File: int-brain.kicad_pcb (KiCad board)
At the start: 2 copper layers, 117.4 x 66.6 mm, 62 parts, among them J1 PWR, J10 Conn_01x19_Pin, J11 Conn_01x19_Pin, J2 UART0, J3 I2C0, J4 PWR, J5 1MA, J6 1MB, J7 2MA, J8 2MB, J9 MPU9250, U1 L298N, U2 ESP32-DevKitC, U3 L298N, U4 LM2576HVT-5

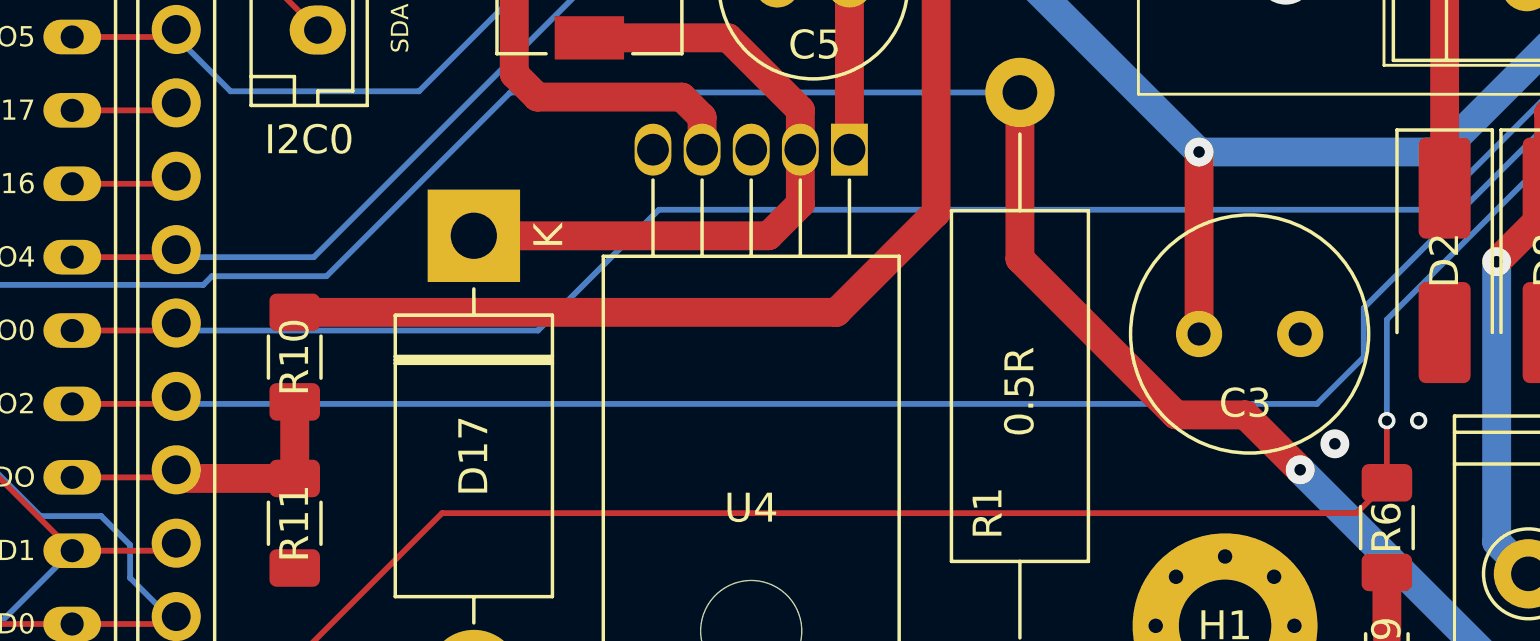
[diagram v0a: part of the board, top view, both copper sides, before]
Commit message: re-do pinouts based on code
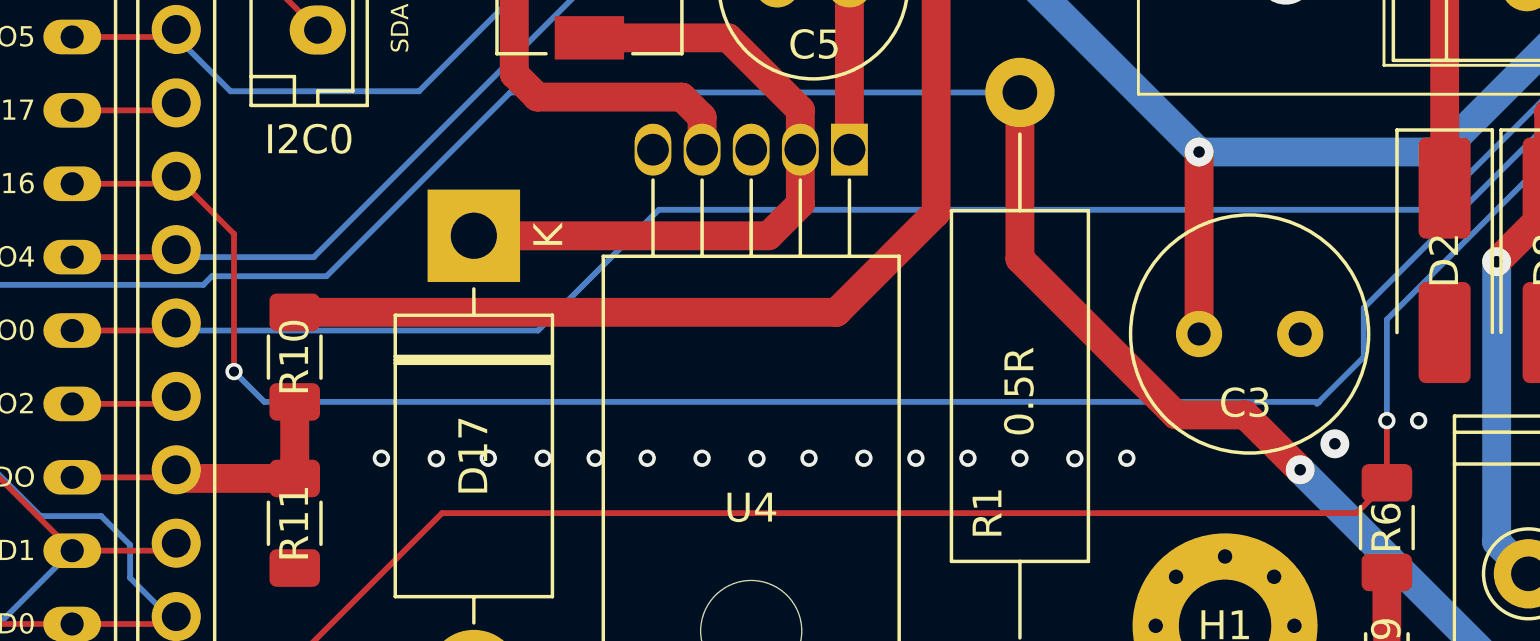
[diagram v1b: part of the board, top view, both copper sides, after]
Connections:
- J11 pad 12: /GPIO16 -> 1MA2_IN
- J11 pad 15: 1MA2_IN -> /GPIO2
- U2 pad 24: 1MA2_IN -> /GPIO2
- U2 pad 27: /GPIO16 -> 1MA2_IN
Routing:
- net 1MA2_IN: track 72.2 -> 78.3 mm, vias 0 -> 1
- net /GPIO2: track 0.00 -> 3.60 mm
- net /GPIO16: track 3.60 -> 0.00 mm
- net GND: vias 54 -> 69

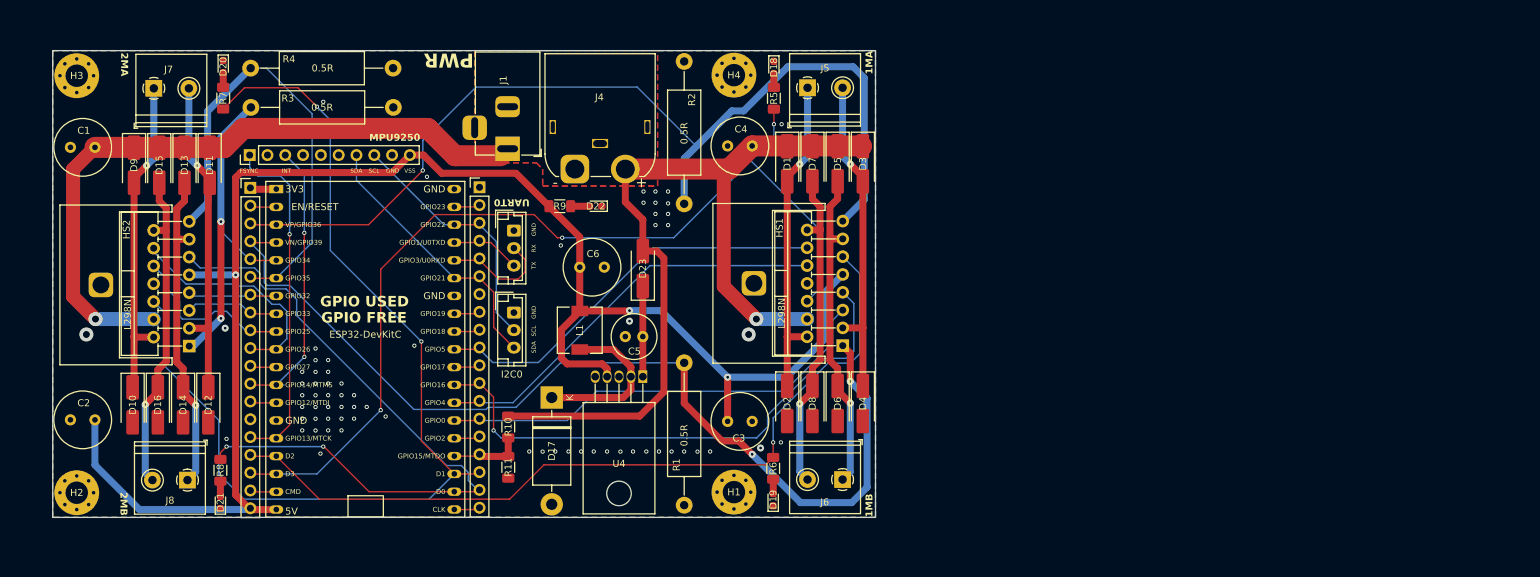
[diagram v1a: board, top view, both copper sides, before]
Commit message: finish schematic rearrangement
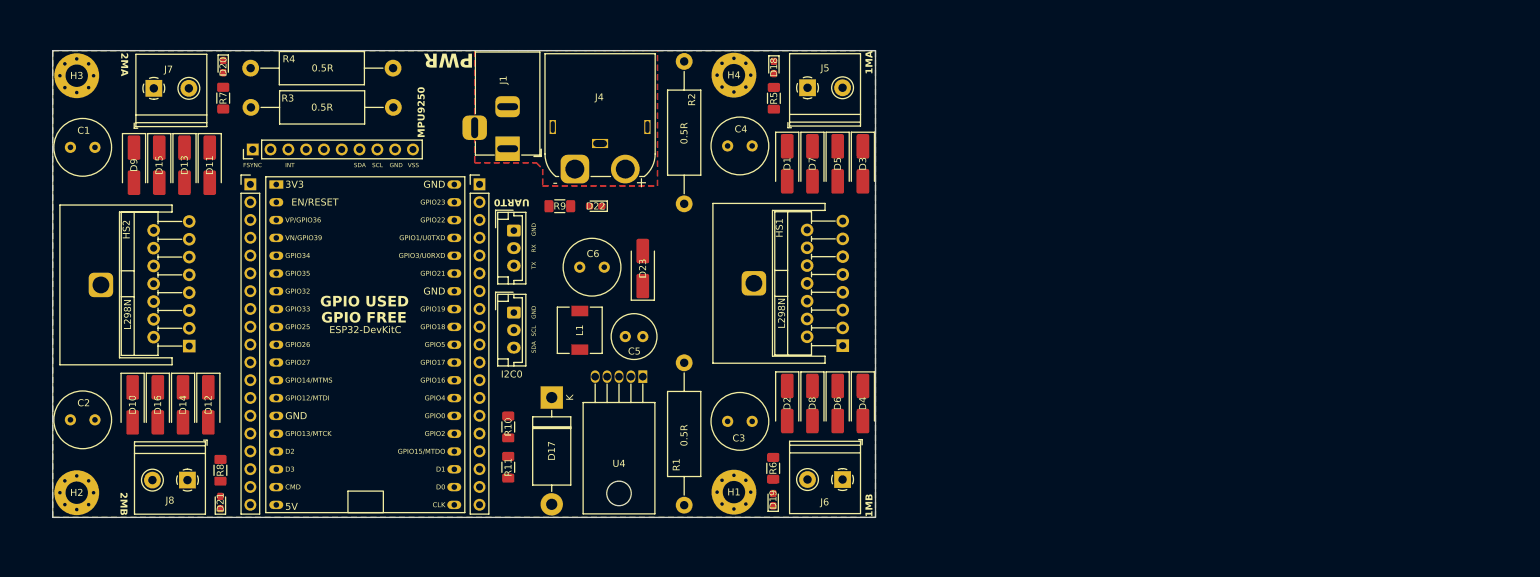
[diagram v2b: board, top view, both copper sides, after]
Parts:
- J10: value Conn_01x19_Pin -> Left
- J11: value Conn_01x19_Pin -> Right
- moved J9 0.91 mm to (88.9, 62.5)
- moved U2 0.66 mm to (92.3, 67.5)
- moved J10 0.50 mm to (88.6, 67.5)
- moved J11 0.42 mm to (121.3, 67.5)
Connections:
- net /CHIP_PU renamed /EN
- net /CMD renamed /GPIO11
- J10 pad 10: 2MB2_IN -> 2MA2_IN
- J10 pad 11: /GPIO27 -> 2MA_EN
- J10 pad 12: INT -> 2MA1_IN
- J10 pad 13: /GPIO12 -> FSYNC
- J10 pad 14: unconnected-(J10-Pin_14-Pad14) -> GND
- J10 pad 15: FSYNC -> INT
- J10 pad 16: 1MB_EN -> /GPIO9
- J10 pad 17: 1MA_EN -> /GPIO10
- J10 pad 3: 1MB_SENSE -> /GPIO36
- J10 pad 4: 1MA_SENSE -> VBATT
- J10 pad 7: 2MA2_IN -> 2MB2_IN
- J10 pad 8: 2MA1_IN -> 2MB_EN
- J11 pad 10: 1MB2_IN -> 1MA2_IN
- J11 pad 11: /GPIO17 -> 1MA_EN
- J11 pad 12: 1MA2_IN -> 1MA1_IN
- J11 pad 13: 1MB1_IN -> 1MB_SENSE
- J11 pad 14: 1MA1_IN -> /GPIO0
- J11 pad 16: VBATT -> 1MA_SENSE
- J11 pad 17: 2MA_EN -> /GPIO8
- J11 pad 18: 2MB_EN -> /GPIO7
- J11 pad 2: /GPIO23 -> 1MB2_IN
- J11 pad 8: /GPIO19 -> 1MB_EN
- J11 pad 9: /GPIO18 -> 1MB1_IN
- U2 pad 10: 2MB2_IN -> 2MA2_IN
- U2 pad 11: /GPIO27 -> 2MA_EN
- U2 pad 12: INT -> 2MA1_IN
- U2 pad 13: /GPIO12 -> FSYNC
- U2 pad 15: FSYNC -> INT
- U2 pad 16: 1MB_EN -> /GPIO9
- U2 pad 17: 1MA_EN -> /GPIO10
- U2 pad 21: 2MB_EN -> /GPIO7
- U2 pad 22: 2MA_EN -> /GPIO8
- U2 pad 23: VBATT -> 1MA_SENSE
- U2 pad 25: 1MA1_IN -> /GPIO0
- U2 pad 26: 1MB1_IN -> 1MB_SENSE
- U2 pad 27: 1MA2_IN -> 1MA1_IN
- U2 pad 28: /GPIO17 -> 1MA_EN
- U2 pad 29: 1MB2_IN -> 1MA2_IN
- U2 pad 3: 1MB_SENSE -> /GPIO36
- U2 pad 30: /GPIO18 -> 1MB1_IN
- U2 pad 31: /GPIO19 -> 1MB_EN
- U2 pad 37: /GPIO23 -> 1MB2_IN
- U2 pad 4: 1MA_SENSE -> VBATT
- U2 pad 7: 2MA2_IN -> 2MB2_IN
- U2 pad 8: 2MA1_IN -> 2MB_EN
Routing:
- net VSS: track 233.2 -> 0.00 mm, vias 3 -> 0
- net VS: track 221.6 -> 0.00 mm, vias 2 -> 0
- net 2MA_EN: track 144.9 -> 0.00 mm, vias 2 -> 0
- net 1MA_SENSE: track 140.7 -> 0.00 mm, vias 2 -> 0
- net 1MA_EN: track 137.9 -> 0.00 mm, vias 3 -> 0
- net 1MB_SENSE: track 137.8 -> 0.00 mm, vias 1 -> 0
- net 1MB_EN: track 116.3 -> 0.00 mm, vias 1 -> 0
- net 2MB_EN: track 99.1 -> 0.00 mm, vias 2 -> 0
- net 1MA2_IN: track 78.3 -> 0.00 mm, vias 1 -> 0
- net 2MA_SENSE: track 66.2 -> 0.00 mm
- net 1MA1_IN: track 63.9 -> 0.00 mm
- net 1MB1_IN: track 58.5 -> 0.00 mm
- net 1MB2_IN: track 57.9 -> 0.00 mm
- net FSYNC: track 49.2 -> 0.00 mm, vias 1 -> 0
- net 2MB_SENSE: track 49.0 -> 0.00 mm, vias 2 -> 0
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
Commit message: finish?
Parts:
- moved R3 5.60 mm to (88.6, 50.9)
- moved R4 5.60 mm to (88.6, 56.5)
- moved D10 0.20 mm to (72.0, 98.9)
- moved D12 0.20 mm to (82.8, 98.9)
- moved D14 0.20 mm to (79.2, 98.9)
- moved D16 0.20 mm to (75.6, 98.9)
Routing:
- net VSS: track 0.00 -> 269.2 mm, vias 0 -> 1
- net VS: track 0.00 -> 216.3 mm, vias 0 -> 3
- net 1MB_EN: track 0.00 -> 125.0 mm, vias 0 -> 1
- net 2MB_SENSE: track 0.00 -> 114.7 mm
- net 1MA_EN: track 0.00 -> 94.6 mm, vias 0 -> 3
- net 1MB_SENSE: track 0.00 -> 92.9 mm
- net 1MA1_IN: track 0.00 -> 69.3 mm
- net 1MA_SENSE: track 0.00 -> 64.9 mm, vias 0 -> 1
- net 2MA_EN: track 0.00 -> 61.9 mm, vias 0 -> 1
- net 1MA2_IN: track 0.00 -> 60.1 mm
- net VBATT: track 0.00 -> 58.6 mm, vias 0 -> 1
- net 1MB1_IN: track 0.00 -> 54.0 mm
- net 1MB2_IN: track 0.00 -> 53.0 mm
- net 2MA_SENSE: track 0.00 -> 50.7 mm
- net INT: track 0.00 -> 47.0 mm
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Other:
- outline, holes or cut-outs redrawn
- board text added: "+"
- board text added: "14-26 27-35"
- board text added: "16-5-17-15"
- board text added: "18-23-19-4"
- board text added: "25-32 33-34"
- board text added: "FSYNC-12"
- board text added: "INT-13"
- board text added: "MOTOR: I1-I2-EN-SE ALLWAYS GPIO"
- board text added: "RX 03"
- board text added: "SCL 22"
- board text added: "SDA 21"
- board text added: "TX 01"
- board text added: "→"
- board text removed: "FSYNC"
- board text removed: "INT"
- board text removed: "RX"
- board text removed: "TX"

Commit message: add formula
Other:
- board text added: "(10 || 5) / 57 VS"
- board text added: "@39"
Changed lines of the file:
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@@
+		)
+	)
+	(gr_text "(10 || 5) / 57 VS"
+		(at 128 111.5 90)
+		(layer "F.SilkS")
+		(effects
+			(font
+				(size 0.8 0.8)
+				(thickness 0.1)
+			)
+			(justify left bottom)
 		)
 	)
@@
 			)
 			(justify left bottom)
+		)
+	)
+	(gr_text "@39"
+		(at 123.5 112 0)
+		(layer "F.SilkS")
+		(effects
+			(font
+				(size 1 1)
+				(thickness 0.1)
+			)
+			(justify left bottom)

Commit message: set current sense resistors
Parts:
- R1, R2, R3, R4: value 0.5R -> 0R33
- R11: value 10k -> 3.9k
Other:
- board text added: "2k OR 3k9 6S OR 3S"
- board text added: "47k"
- board text removed: "(10 || 5) / 57 VS"
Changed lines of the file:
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@@
 			)
 		)
-		(property "Value" "10k"
+		(property "Value" "3.9k"
 			(at 0 1.82 90)
 			(layer "F.Fab")
@@
 			)
 		)
-		(property "Value" "0.5R"
+		(property "Value" "0R33"
 			(at 10.16 0 0)
 			(layer "F.SilkS")
@@
 			)
 		)
-		(property "Value" "0.5R"
+		(property "Value" "0R33"
 			(at 10.06 0 -90)
 			(layer "F.SilkS")
@@
 			)
 		)
-		(property "Value" "0.5R"
+		(property "Value" "0R33"
 			(at 10.36 0 90)
 			(layer "F.SilkS")
@@
 			)
 		)
-		(property "Value" "0.5R"
+		(property "Value" "0R33"
 			(at 10.26 0 0)
 			(layer "F.SilkS")
@@
 		)
 	)
-	(gr_text "(10 || 5) / 57 VS"
-		(at 128 111.5 90)
+	(gr_text "2k OR 3k9\n6S OR 3S"
+		(at 128.6 110.8 90)
 		(layer "F.SilkS")
 		(effects
 			(font
-				(size 0.8 0.8)
-				(thickness 0.1)
+				(size 0.7 0.7)
+				(thickness 0.0875)
 			)
 			(justify left bottom)
@@
 			)
 			(justify left bottom)
+		)
+	)
+	(gr_text "47k"
+		(at 128 103.1 90)
+		(layer "F.SilkS")
+		(effects
+			(font
+				(size 0.7 0.7)
+				(thickness 0.0875)
+			)
+			(justify left bottom)

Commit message: done placement
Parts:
- added C7: 100uF, Capacitor_THT:C_Radial_D6.3mm_H11.0mm_P2.50mm, F.Cu at (161.2, 82.7)
- added C8: 1mF, Capacitor_THT:C_Radial_D8.0mm_H11.5mm_P3.50mm, F.Cu at (143.0, 73.4)
- added D24: 1N5822, Diode_THT:D_DO-201AD_P15.24mm_Horizontal, F.Cu at (150.5, 91.5)
- added D25: PWR, LED_SMD:LED_0603_1608Metric_Pad1.05x0.95mm_HandSolder, F.Cu at (144.5, 91.9)
- added J12: 1MA_ENC, Connector_JST:JST_EH_B4B-EH-A_1x04_P2.50mm_Vertical, F.Cu at (177.8, 47.1)
- added J13: 1MB_ENC, Connector_JST:JST_EH_B4B-EH-A_1x04_P2.50mm_Vertical, F.Cu at (177.3, 107.1)
- added J14: 2MA_ENC, Connector_JST:JST_EH_B4B-EH-A_1x04_P2.50mm_Vertical, F.Cu at (89.3, 46.7)
- added J15: 2MB_ENC, Connector_JST:JST_EH_B4B-EH-A_1x04_P2.50mm_Vertical, F.Cu at (88.3, 107.2)
- added J16: USB_A, Connector_USB:USB_A_Molex_67643_Horizontal, F.Cu at (133.9, 98.0)
- added JP1: SolderJumper_2_Open, Jumper:SolderJumper-2_P1.3mm_Open_Pad1.0x1.5mm, B.Cu at (129.4, 45.6)
- added JP2: SolderJumper_2_Open, Jumper:SolderJumper-2_P1.3mm_Open_Pad1.0x1.5mm, B.Cu at (129.4, 48.1)
- added JP3: SolderJumper_2_Open, Jumper:SolderJumper-2_P1.3mm_Open_Pad1.0x1.5mm, B.Cu at (129.4, 50.6)
- added JP4: SolderJumper_2_Open, Jumper:SolderJumper-2_P1.3mm_Open_Pad1.0x1.5mm, B.Cu at (129.4, 53.1)
- added JP5: SolderJumper_2_Open, Jumper:SolderJumper-2_P1.3mm_Open_Pad1.0x1.5mm, B.Cu at (103.4, 45.4)
- added L2: 100mH, Inductor_SMD:L_6.3x6.3_H3, F.Cu at (150.8, 82.2)
- added R12: 10k, Resistor_SMD:R_1206_3216Metric_Pad1.30x1.75mm_HandSolder, B.Cu at (191.5, 53.8)
- added R13: 10k, Resistor_SMD:R_1206_3216Metric_Pad1.30x1.75mm_HandSolder, B.Cu at (81.8, 50.2)
- added R14: 10k, Resistor_SMD:R_1206_3216Metric_Pad1.30x1.75mm_HandSolder, B.Cu at (193.2, 100.6)
- added R15: 10k, Resistor_SMD:R_1206_3216Metric_Pad1.30x1.75mm_HandSolder, B.Cu at (81.8, 103.7)
- added R16: 4.7k, Resistor_SMD:R_1206_3216Metric_Pad1.30x1.75mm_HandSolder, B.Cu at (117.5, 65.9)
- added R17: 4.7k, Resistor_SMD:R_1206_3216Metric_Pad1.30x1.75mm_HandSolder, B.Cu at (117.5, 73.7)
- added R18: 10k, Resistor_SMD:R_1206_3216Metric_Pad1.30x1.75mm_HandSolder, B.Cu at (123.9, 45.6)
- added R19: 10k, Resistor_SMD:R_1206_3216Metric_Pad1.30x1.75mm_HandSolder, B.Cu at (123.9, 48.1)
- added R20: 10k, Resistor_SMD:R_1206_3216Metric_Pad1.30x1.75mm_HandSolder, B.Cu at (123.9, 50.6)
- added R21: 10k, Resistor_SMD:R_1206_3216Metric_Pad1.30x1.75mm_HandSolder, B.Cu at (123.9, 53.1)
- added R22: 10k, Resistor_SMD:R_1206_3216Metric_Pad1.30x1.75mm_HandSolder, B.Cu at (98.6, 45.4)
- added R23: 470R, Resistor_SMD:R_1206_3216Metric_Pad1.30x1.75mm_HandSolder, F.Cu at (139.5, 91.9)
- added SW1: SW_Push, Button_Switch_THT:SW_PUSH_6mm_H5mm, F.Cu at (144.5, 80.7)
- added U5: 74LVC2G04, Package_TO_SOT_SMD:SOT-23-6_Handsoldering, B.Cu at (183.2, 77.1)
- added U6: 74LVC2G04, Package_TO_SOT_SMD:SOT-23-6_Handsoldering, B.Cu at (81.3, 76.2)
- added U7: PCA9635, Package_SO:TSSOP-28_4.4x9.7mm_P0.65mm, B.Cu at (114.6, 49.6)
- added U8: LM2576HVT-5, Package_TO_SOT_THT:TO-220-5_Horizontal_TabDown, F.Cu at (163.4, 88.9)
- R1, R2, R3, R4: value 0R33 -> 0.5R
- R10: moved to B.Cu
- R11: value 3.9k -> 10k; moved to B.Cu
- moved H3 137.8 mm to (190.2, 106.9)
- moved H1 99.3 mm to (58.4, 106.9)
- moved H2 64.5 mm to (58.4, 47.2)
- moved D17 38.1 mm to (169.2, 91.6)
- moved R3 38.0 mm to (83.3, 88.6), turned to -90 degrees
- moved U4 37.6 mm to (165.1, 63.4), turned to 0 degrees
- moved L1 34.0 mm to (168.8, 80.9)
- moved C6 33.5 mm to (168.0, 70.9)
- moved C3 33.3 mm to (193.2, 96.7)
- moved C4 33.3 mm to (189.7, 57.4)
- moved D1 33.3 mm to (198.2, 59.9)
- moved D18 33.3 mm to (196.3, 46.2)
- moved D19 33.3 mm to (196.2, 107.8)
- moved D2 33.3 mm to (198.2, 94.1)
- moved D3 33.3 mm to (209.0, 59.9)
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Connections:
- net /BUCK_OUT renamed /BUCK_OUT_1
- net /PWR_LED renamed /PWR_LED_1
- net /VIN_BUCK renamed VIN_BUCK
- J10 pad 10: 2MA2_IN -> /2MA1_ENC
- J10 pad 11: 2MA_EN -> /2MA2_ENC
- J10 pad 12: 2MA1_IN -> /2MB1_ENC
- J10 pad 13: FSYNC -> /2MB2_ENC
- J10 pad 15: INT -> /GPIO13
- J10 pad 3: /GPIO36 -> 2MB_SENSE
- J10 pad 4: VBATT -> 2MA_SENSE
- J10 pad 5: 2MB_SENSE -> 1MB_SENSE
- J10 pad 6: 2MA_SENSE -> 1MA_SENSE
- J10 pad 7: 2MB2_IN -> FSYNC
- J10 pad 8: 2MB_EN -> INT
- J10 pad 9: 2MB1_IN -> VBATT
- J11 pad 10: 1MA2_IN -> /1MB2_ENC
- J11 pad 11: 1MA_EN -> /1MB1_ENC
- J11 pad 12: 1MA1_IN -> /GPIO16
- J11 pad 13: 1MB_SENSE -> M_OE
- J11 pad 16: 1MA_SENSE -> /GPIO15
- J11 pad 2: 1MB2_IN -> /GPIO23
- J11 pad 8: 1MB_EN -> /1MA1_ENC
- J11 pad 9: 1MB1_IN -> /1MA2_ENC
- R5 pad 1: 1MA_EN -> /1MA_EN
- R6 pad 1: 1MB_EN -> /1MB_EN
- R7 pad 1: 2MA_EN -> /2MA_EN
- R8 pad 1: 2MB_EN -> /2MB_EN
- U1 pad 10: 1MB1_IN -> /1MB1_IN
- U1 pad 11: 1MB_EN -> /1MB_EN
- U1 pad 12: 1MB2_IN -> Net-(U1-IN4)
- U1 pad 5: 1MA1_IN -> /1MA1_IN
- U1 pad 6: 1MA_EN -> /1MA_EN
- U1 pad 7: 1MA2_IN -> Net-(U1-IN2)
- U2 pad 10: 2MA2_IN -> /2MA1_ENC
- U2 pad 11: 2MA_EN -> /2MA2_ENC
- U2 pad 12: 2MA1_IN -> /2MB1_ENC
- U2 pad 13: FSYNC -> /2MB2_ENC
- U2 pad 15: INT -> /GPIO13
- U2 pad 23: 1MA_SENSE -> /GPIO15
- U2 pad 26: 1MB_SENSE -> M_OE
- U2 pad 27: 1MA1_IN -> /GPIO16
- U2 pad 28: 1MA_EN -> /1MB1_ENC
- U2 pad 29: 1MA2_IN -> /1MB2_ENC
- U2 pad 3: /GPIO36 -> 2MB_SENSE
- U2 pad 30: 1MB1_IN -> /1MA2_ENC
- U2 pad 31: 1MB_EN -> /1MA1_ENC
- U2 pad 37: 1MB2_IN -> /GPIO23
- U2 pad 4: VBATT -> 2MA_SENSE
- U2 pad 5: 2MB_SENSE -> 1MB_SENSE
- U2 pad 6: 2MA_SENSE -> 1MA_SENSE
- U2 pad 7: 2MB2_IN -> FSYNC
- U2 pad 8: 2MB_EN -> INT
- U2 pad 9: 2MB1_IN -> VBATT
- U3 pad 10: 2MB1_IN -> /2MB1_IN
- U3 pad 11: 2MB_EN -> /2MB_EN
- U3 pad 12: 2MB2_IN -> Net-(U3-IN4)
- U3 pad 5: 2MA1_IN -> /2MA1_IN
- U3 pad 6: 2MA_EN -> /2MA_EN
- U3 pad 7: 2MA2_IN -> Net-(U3-IN2)
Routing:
- net VSS: track 269.2 -> 0.00 mm, vias 1 -> 0
- net VS: track 216.3 -> 0.00 mm, vias 3 -> 0
- net 1MB_EN: track 125.0 -> 0.00 mm, vias 1 -> 0
- net 2MB_SENSE: track 114.7 -> 0.40 mm
- net 1MA_EN: track 94.6 -> 0.00 mm, vias 3 -> 0
- net 1MB_SENSE: track 92.9 -> 0.00 mm
- net 1MA1_IN: track 69.3 -> 0.00 mm
- net 1MA_SENSE: track 64.9 -> 0.00 mm, vias 1 -> 0
- net 2MA_EN: track 61.9 -> 0.00 mm, vias 1 -> 0
- net 1MA2_IN: track 60.1 -> 0.00 mm
- net VBATT: track 58.6 -> 0.00 mm, vias 1 -> 0
- net 1MB1_IN: track 54.0 -> 0.00 mm
- net 1MB2_IN: track 53.0 -> 0.00 mm
- net 2MA_SENSE: track 50.7 -> 0.00 mm
- net INT: track 47.0 -> 0.00 mm
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- removed copper zone on B.Cu, net GND
- removed copper zone on F.Cu, net GND
- removed copper zone on F.Cu, net VS
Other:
- board size 117.4 x 66.6 mm -> 160.8 x 66.6 mm
